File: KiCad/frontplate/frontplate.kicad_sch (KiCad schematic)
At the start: 4 parts

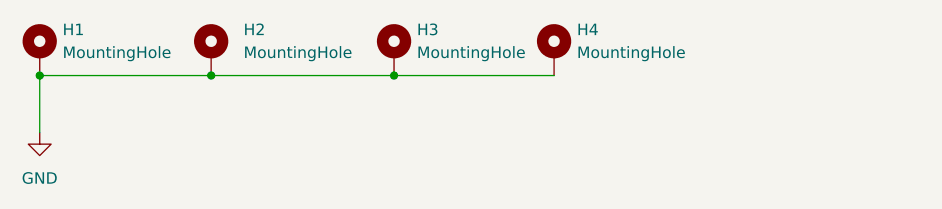
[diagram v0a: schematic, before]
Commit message: Modify for EMF camp - Change shape - Move standoffs to bottom PCB - Add RGB LEDs and power conversion for them - Add art - Generate and add 3D models
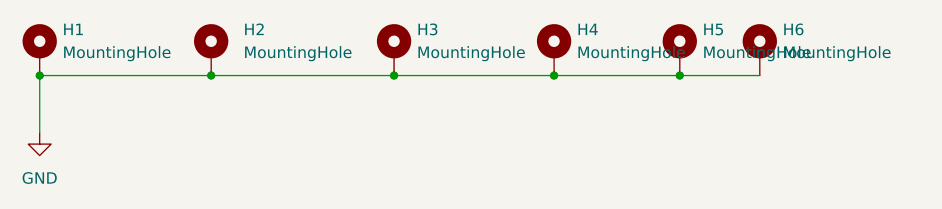
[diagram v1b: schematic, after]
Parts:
- added H5, H6: MountingHole, MountingHole:MountingHole_2.2mm_M2, symbol Mechanical:MountingHole_Pad
- H1, H2, H3, H4: footprint frontplate:SMTSO2020CTJ -> MountingHole:MountingHole_2.2mm_M2
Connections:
- net GND: now also H5.1, H6.1
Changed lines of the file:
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@@
+	)
+	(junction
+		(at 107.95 30.48)
+		(diameter 0)
+		(color 0 0 0 0)
 	)
 	(junction
@@
 	)
 	(junction
+		(at 93.98 30.48)
+		(diameter 0)
+		(color 0 0 0 0)
+	)
+	(junction
 		(at 76.2 30.48)
 		(diameter 0)
@@
 	(wire
 		(pts
-			(xy 93.98 30.48) (xy 76.2 30.48)
+			(xy 107.95 30.48) (xy 93.98 30.48)
 		)
 		(stroke
@@
 	(wire
 		(pts
-			(xy 55.88 30.48) (xy 36.83 30.48)
+			(xy 116.84 30.48) (xy 107.95 30.48)
 		)
 		(stroke
@@
 		)
 	)
+	(wire
+		(pts
+			(xy 93.98 30.48) (xy 76.2 30.48)
+		)
+		(stroke
+			(width 0)
+			(type default)
+		)
+	)
+	(wire
+		(pts
+			(xy 55.88 30.48) (xy 36.83 30.48)
+		)
+		(stroke
+			(width 0)
+			(type default)
+		)
+	)
 	(symbol
 		(lib_id "Mechanical:MountingHole_Pad")
@@
 			)
 		)
-		(property "Footprint" "frontplate:SMTSO2020CTJ"
+		(property "Footprint" "MountingHole:MountingHole_2.2mm_M2"
 			(at 55.88 27.94 0)
 			(effects
@@
 			)
 		)
-		(property "Footprint" "frontplate:SMTSO2020CTJ"
+		(property "Footprint" "MountingHole:MountingHole_2.2mm_M2"
 			(at 93.98 27.94 0)
 			(effects
@@
 			)
 		)
-		(property "Footprint" "frontplate:SMTSO2020CTJ"
+		(property "Footprint" "MountingHole:MountingHole_2.2mm_M2"
 			(at 36.83 27.94 0)
 			(effects
@@
 			)
 		)
-		(property "Footprint" "frontplate:SMTSO2020CTJ"
+		(property "Footprint" "MountingHole:MountingHole_2.2mm_M2"
 			(at 76.2 27.94 0)
 			(effects
@@
 					(unit 1)
 				)
+			)
+		)
+	)
+	(symbol
+		(lib_id "Mechanical:MountingHole_Pad")
+		(at 116.84 27.94 0)
+		(unit 1)
+		(exclude_from_sim no)
+		(in_bom no)
+		(on_board yes)
+		(dnp no)
+		(fields_autoplaced yes)
+		(property "Reference" "H6"
+			(at 119.38 25.3999 0)
+			(effects
+				(font
+					(size 1.27 1.27)
+				)
+				(justify left)
+			)
+		)
+		(property "Value" "MountingHole"
+			(at 119.38 27.9399 0)
+			(effects
+				(font
+					(size 1.27 1.27)
+				)
+				(justify left)
+			)
+		)
+		(property "Footprint" "MountingHole:MountingHole_2.2mm_M2"
+			(at 116.84 27.94 0)
+			(effects
+				(font
+					(size 1.27 1.27)
+				)
+				(hide yes)
+			)
+		)
+		(property "Datasheet" "~"
+			(at 116.84 27.94 0)
+			(effects
+				(font
+					(size 1.27 1.27)
+				)
+				(hide yes)
+			)
+		)
+		(property "Description" "Mounting Hole with connection"
+			(at 116.84 27.94 0)
+			(effects
+				(font
+					(size 1.27 1.27)
+				)
+				(hide yes)
+			)
+		)
+		(pin "1"
+		)
+		(instances
+			(project "frontplate"
+				(path "/9e0e3ef3-79e5-41ac-8b6e-50a08cbcb74d"
+					(reference "H6")
+					(unit 1)
+				)
+			)
+		)
+	)
+	(symbol
+		(lib_id "Mechanical:MountingHole_Pad")
+		(at 107.95 27.94 0)
+		(unit 1)
+		(exclude_from_sim no)
+		(in_bom no)
+		(on_board yes)
+		(dnp no)
+		(fields_autoplaced yes)
+		(property "Reference" "H5"
+			(at 110.49 25.3999 0)
+			(effects
+				(font
+					(size 1.27 1.27)
+				)
+				(justify left)
+			)
+		)
+		(property "Value" "MountingHole"
+			(at 110.49 27.9399 0)
+			(effects
+				(font
+					(size 1.27 1.27)
+				)
+				(justify left)
+			)
+		)
+		(property "Footprint" "MountingHole:MountingHole_2.2mm_M2"
+			(at 107.95 27.94 0)
+			(effects
+				(font
+					(size 1.27 1.27)
+				)
+				(hide yes)
+			)
+		)
+		(property "Datasheet" "~"
+			(at 107.95 27.94 0)
+			(effects
+				(font
+					(size 1.27 1.27)
+				)
+				(hide yes)
+			)
+		)
+		(property "Description" "Mounting Hole with connection"
+			(at 107.95 27.94 0)
+			(effects
+				(font
+					(size 1.27 1.27)
+				)
+				(hide yes)
+			)
+		)
+		(pin "1"
+		)
+		(instances
+			(project "frontplate"
+				(path "/9e0e3ef3-79e5-41ac-8b6e-50a08cbcb74d"
+					(reference "H5")
+					(unit 1)
+				)
